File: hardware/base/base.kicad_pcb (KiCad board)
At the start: 4 copper layers, 60 x 60 mm, 73 parts, among them J1 Debug, J2 USB_B_Mini, J3 Serial Interface, J4 SWD, J5 OLED Display, M1 Fan_ALT, Q1 Q_NMOS_GSD, Q2 Q_NMOS_GSD, Q3 Q_NMOS_GSD, SW3 RotaryEncoder_Switch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

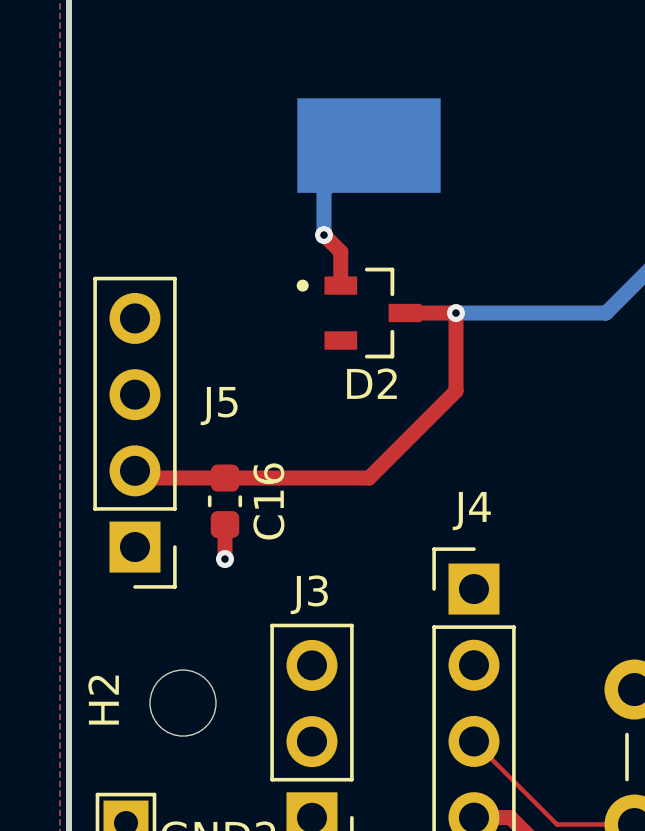
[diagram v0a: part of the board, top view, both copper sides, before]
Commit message: Add pull-up resistors to display
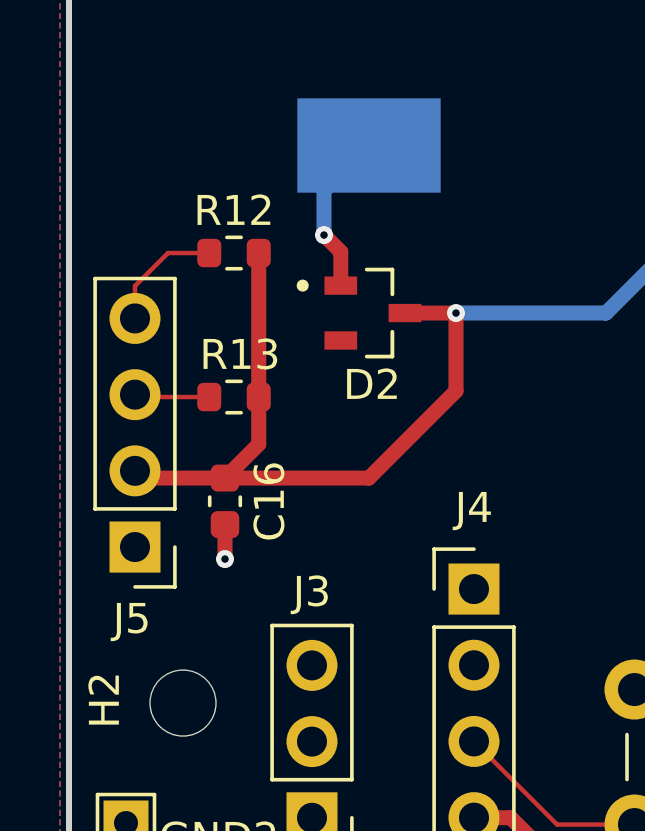
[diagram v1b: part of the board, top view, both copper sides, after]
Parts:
- added R12: 10k, Resistor_SMD:R_0603_1608Metric, F.Cu at (125.8, 59.0)
- added R13: 10k, Resistor_SMD:R_0603_1608Metric, F.Cu at (125.8, 63.8)
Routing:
- net +3.3V: track 136.5 -> 144.5 mm
- net Net-(J5-Pin_4): track 33.5 -> 37.5 mm
- net Net-(J5-Pin_3): track 32.6 -> 35.1 mm
